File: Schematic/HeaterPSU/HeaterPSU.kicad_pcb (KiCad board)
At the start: 2 copper layers, 100 x 35 mm, 59 parts, among them J201 SMPS2_SEC, J202 Heater Output, J203 Heater Control, J204 MCU_Interface, J205 High voltage warning, K201 Relay_TE_OJT_SH_124DM, Q201 IRF4905, Q202 BSS138, SW201 SW_Rotary_1P5T_ALPSALPINE_SRBV, U201 TPS54302, U202 TLP185, U203 TLP185

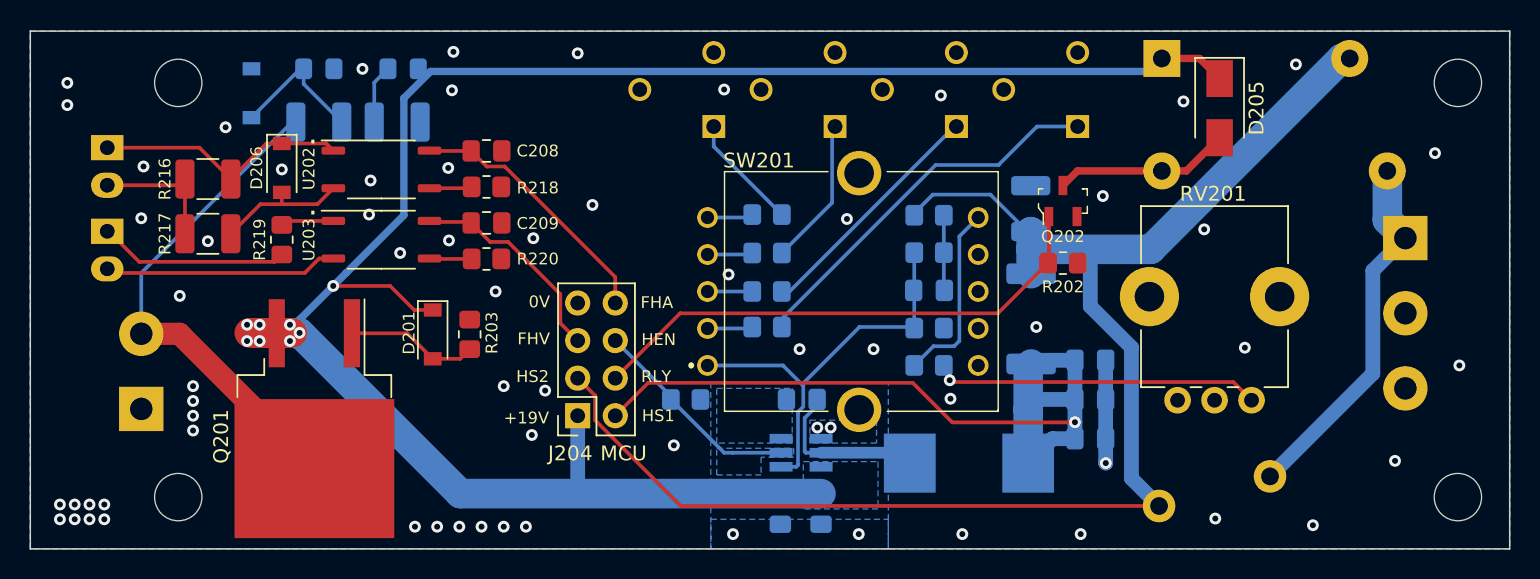
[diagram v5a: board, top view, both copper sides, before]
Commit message: Optocouplers moved to from PSU to MCU board
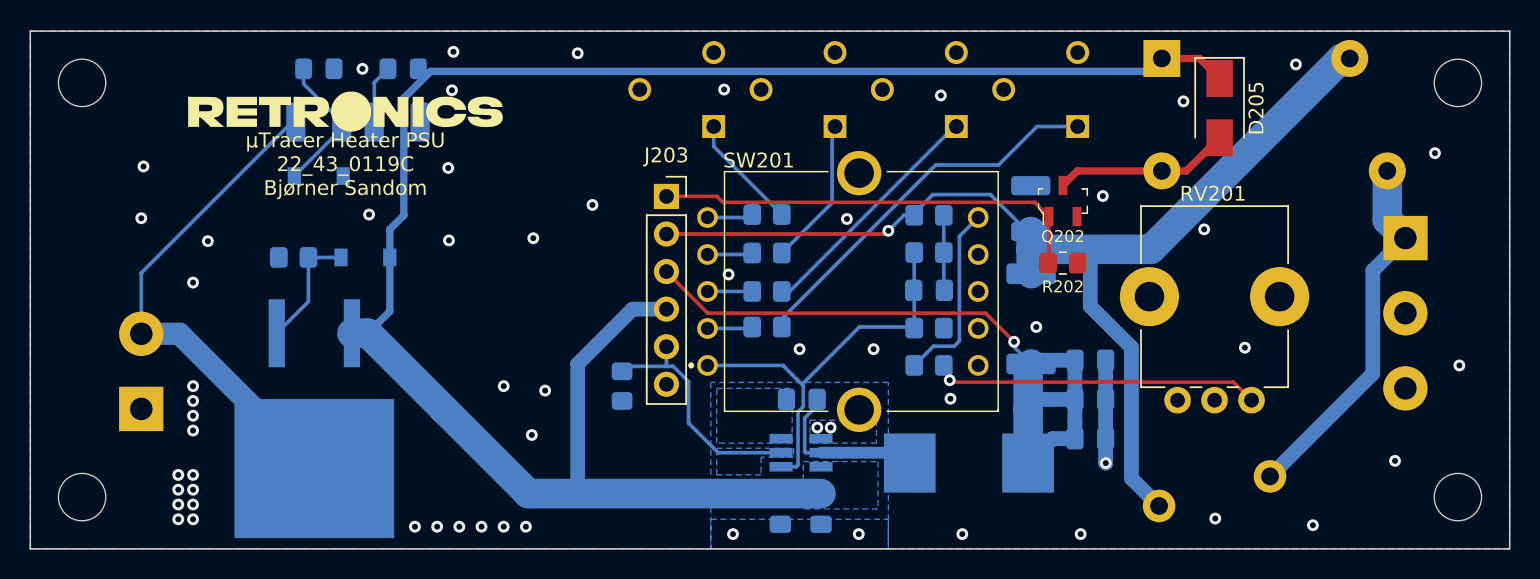
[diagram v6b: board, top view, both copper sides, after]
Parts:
- removed C208, C209: 220nF, Capacitor_SMD:C_0805_2012Metric_Pad1.18x1.45mm_HandSolder
- removed D206: 1N4148W, Diode_SMD:D_SOD-123
- removed J204: MCU_Interface, Connector_PinSocket_2.54mm:PinSocket_2x04_P2.54mm_Vertical
- removed J205: High voltage warning, myDevices:KF2510-2P
- removed R216, R217: 3.9kΩ 1/2W, Resistor_SMD:R_1210_3225Metric_Pad1.30x2.65mm_HandSolder
- removed R218, R219, R220: 220Ω, Resistor_SMD:R_0805_2012Metric_Pad1.20x1.40mm_HandSolder
- removed U202, U203: TLP185, Package_SO:SOIC-4_4.55x3.7mm_P2.54mm
- D201, Q201, R203: moved to B.Cu
- G***: moved to F.Cu
- J203: value Heater Control -> Conn_01x06; footprint myDevices:KF2510-2P -> Connector_PinSocket_2.54mm:PinSocket_1x06_P2.54mm_Vertical; moved to F.Cu
- moved J203 37.9 mm to (98.0, 56.2), turned to 0 degrees
- moved G*** 13.7 mm to (76.3, 50.4), turned to 0 degrees
- moved R203 13.0 mm to (72.8, 60.3), turned to 0 degrees
- moved D204 7.22 mm to (74.5, 54.8), turned to 180 degrees
- moved D201 6.91 mm to (77.7, 60.3), turned to 180 degrees
- moved H201 6.50 mm to (58.5, 48.5)
- moved H202 6.50 mm to (58.5, 76.5)
- moved R209 4.39 mm to (95.0, 69.0), turned to 90 degrees
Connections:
- J203 pad 1: Net-(D206-Pad1) -> RLY_CTRL
- J203 pad 2: Net-(J203-Pad2) -> HeaterSense2
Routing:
- net HeaterSense2: track 102.6 -> 76.0 mm, vias 0 -> 1
- net FlagMBHeaterActive: track 17.8 -> 0.00 mm
- net Net-(D206-Pad1): track 17.4 -> 0.00 mm
- net Net-(J205-Pad2): track 15.8 -> 0.00 mm
- net FlagHighVoltage: track 14.3 -> 0.00 mm
- net Net-(J205-Pad1): track 12.9 -> 0.00 mm
- net Net-(J203-Pad2): track 9.12 -> 0.00 mm
- net Net-(D206-Pad2): track 9.03 -> 0.00 mm
- net VDC: track 134.3 -> 126.3 mm, vias 8 -> 0
- net RLY_CTRL: track 35.7 -> 29.6 mm
- net HeaterSense1: track 55.6 -> 49.9 mm
- net Net-(R219-Pad1): track 3.60 -> 0.00 mm
- net Net-(R220-Pad2): track 2.82 -> 0.00 mm
- net Net-(R218-Pad2): track 2.76 -> 0.00 mm
- net Heater_EN: track 14.5 -> 16.3 mm
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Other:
- board text removed: "+ -"
- board text removed: "+19V"
- board text removed: "0V"
- board text removed: "FHA"
- board text removed: "FHV"
- board text removed: "HEN"
- board text removed: "HS1"
- board text removed: "HS2"
- board text removed: "HV LED"
- board text removed: "MB Heater"
- board text removed: "MCU"
- board text removed: "RLY"

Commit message: Added PWM controlled MOSFET output for soft start
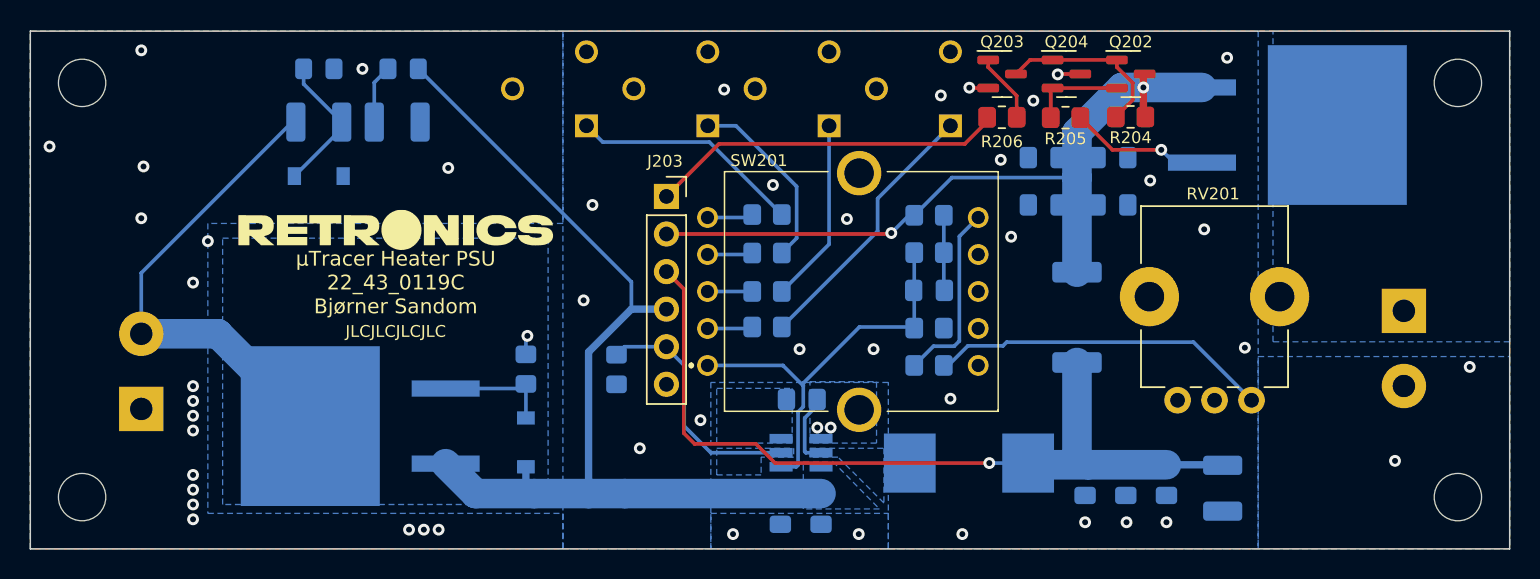
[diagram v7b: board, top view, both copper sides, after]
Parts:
- removed D205: MRA4005T3G, Diode_SMD:D_SMA
- removed K201: Relay_TE_OJT_SH_124DM, myDevices:Relay_TE_OJT_SH_124
- removed the R202 at (124.8, 60.7)
- removed the R209 at (95.0, 69.0)
- removed TH201: 25Ω 3.4A, myDevices:RV_Disc_D15.5mm_W4.5mm_P7.5mm
- added C201: 22µF 25V, Capacitor_SMD:C_0805_2012Metric_Pad1.18x1.45mm_HandSolder, B.Cu at (128.2, 53.5)
- added C203: 22µF 25V, Capacitor_SMD:C_0805_2012Metric_Pad1.18x1.45mm_HandSolder, B.Cu at (123.5, 56.8)
- added C204: 22µF 25V, Capacitor_SMD:C_0805_2012Metric_Pad1.18x1.45mm_HandSolder, B.Cu at (123.5, 53.5)
- added C206: 22µF 25V, Capacitor_SMD:C_0805_2012Metric_Pad1.18x1.45mm_HandSolder, B.Cu at (131.8, 75.3)
- added Q203: BC847, Package_TO_SOT_SMD:SOT-23, F.Cu at (120.7, 47.9)
- added Q204: BC857, Package_TO_SOT_SMD:SOT-23, F.Cu at (125.0, 47.9)
- added Q205: IRF9540N, Package_TO_SOT_SMD:TO-263-2, B.Cu at (140.0, 51.4)
- added R204: 4.7kΩ, Resistor_SMD:R_0805_2012Metric_Pad1.20x1.40mm_HandSolder, F.Cu at (129.4, 50.8)
- added R205: 100Ω, Resistor_SMD:R_0805_2012Metric_Pad1.20x1.40mm_HandSolder, F.Cu at (125.0, 50.9)
- added R206: 1kΩ, Resistor_SMD:R_0805_2012Metric_Pad1.20x1.40mm_HandSolder, F.Cu at (120.7, 50.8)
- added R211: 100kΩ, Resistor_SMD:R_0805_2012Metric_Pad1.20x1.40mm_HandSolder, B.Cu at (94.6, 67.9)
- J202: footprint myDevices:TerminalBlock_LCSC_P5.08mm_3 -> myDevices:TerminalBlock_LCSC_P5.08mm
- J203: value Conn_01x06 -> To MCU Board
- Q202: value BSS138 -> BC847; footprint digikey-footprints:SOT-23-3 -> Package_TO_SOT_SMD:SOT-23
- moved R208 22.9 mm to (135.6, 75.9), turned to -90 degrees
- moved R202 17.4 mm to (88.5, 67.8), turned to -90 degrees
- moved D201 16.6 mm to (88.5, 72.8), turned to 90 degrees
- moved C202 13.2 mm to (128.2, 56.8)
- moved Q202 9.73 mm to (129.4, 47.9), turned to 0 degrees
- moved G*** 8.69 mm to (79.7, 58.4)
- moved RV204 8.60 mm to (109.0, 51.4)
- moved RV205 8.60 mm to (117.2, 51.4)
- moved RV202 8.60 mm to (92.6, 51.4)
- moved RV203 8.60 mm to (100.8, 51.4)
- moved C208 8.11 mm to (126.3, 75.3), turned to 90 degrees
- moved J202 4.92 mm to (147.8, 63.9)
- moved C207 3.69 mm to (129.1, 75.3), turned to 90 degrees
- moved Q201 3.14 mm to (77.3, 71.7), turned to 180 degrees
- moved R207 3.10 mm to (125.8, 64.3)
- renumbered C201 to C205, C203 to C207, C204 to C208, C205 to C209, C206 to C210, C207 to C211, R203 to R202, R204 to R203, R205 to R207, R207 to R208, R206 to R209, R208 to R210, R210 to R212, R211 to R213, R212 to R214, R213 to R215, R214 to R216, R215 to R217
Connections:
- C202 pad 2: HeaterSense1 -> HeaterSense2
- J203 pad 1: RLY_CTRL -> Heater_PWM
- Q202 pad 1: RLY_CTRL -> Net-(Q202-Pad1)
- Q202 pad 2: GNDPWR -> Net-(Q202-Pad2)
- Q202 pad 3: Net-(D205-Pad2) -> HeaterSense2
- R208 pad 1: HeaterSense2 -> HeaterSense1
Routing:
- net VDC: track 126.3 -> 66.5 mm
- net RLY_CTRL: track 29.6 -> 0.00 mm
- net /HeaterOutput: track 24.9 -> 0.00 mm
- net HeaterSense2: track 76.0 -> 51.1 mm, vias 1 -> 2
- net Heater_PWM: track 0.00 -> 24.1 mm
- net Net-(Q202-Pad1): track 0.00 -> 12.0 mm
- net Net-(D205-Pad2): track 11.9 -> 0.00 mm
- net Net-(Q205-Pad1): track 0.00 -> 9.48 mm, vias 0 -> 1
- net Net-(R214-Pad2): track 7.86 -> 15.7 mm
- net Net-(R217-Pad2): track 25.9 -> 18.3 mm
- net Net-(Q202-Pad2): track 0.00 -> 6.40 mm
- net Net-(C205-Pad1): track 11.3 -> 5.01 mm
- net HeaterSense1: track 49.9 -> 54.9 mm
- net Net-(Q203-Pad1): track 0.00 -> 4.67 mm
- net Net-(R216-Pad2): track 16.4 -> 12.5 mm
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- added copper zone on B.Cu, net /HeaterOutput
- added copper zone on B.Cu, net Net-(C205-Pad1)
- added copper zone on B.Cu, net Net-(J201-Pad2)
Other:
- board text removed: "C F2 F1"

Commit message: Added 12V regulator for PWM output driver
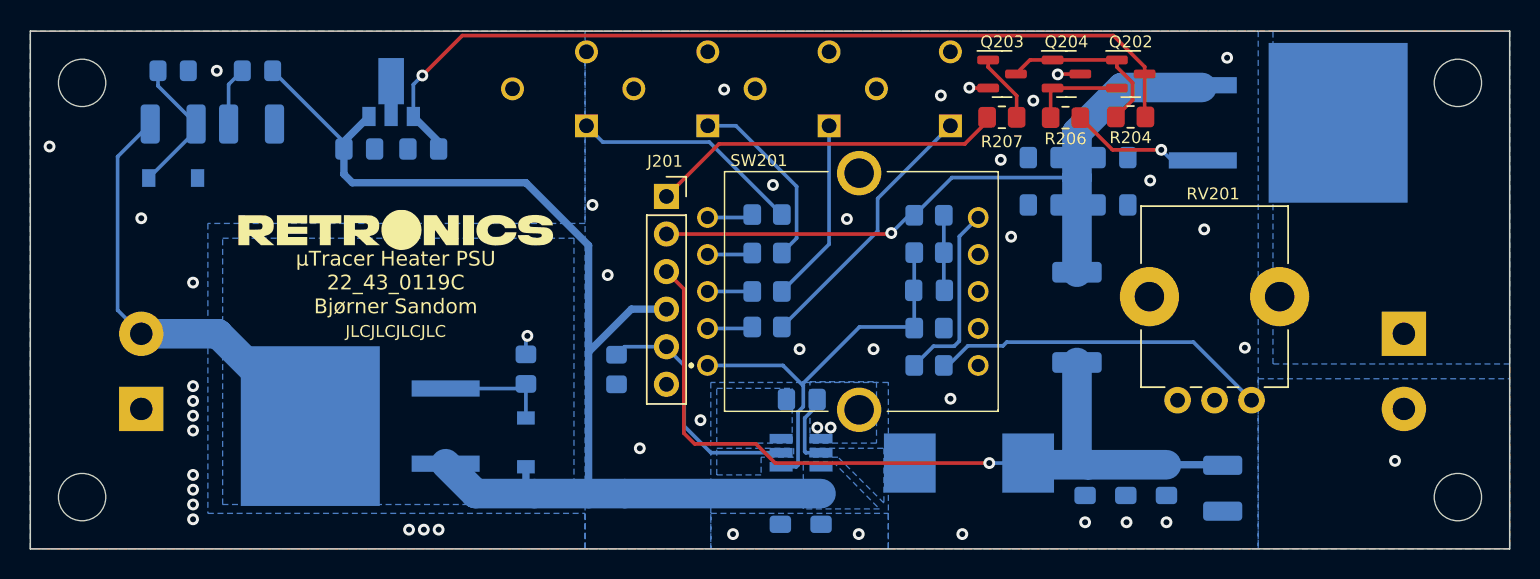
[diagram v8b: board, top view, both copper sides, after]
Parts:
- added C201: 10µF 50V, Capacitor_SMD:C_0805_2012Metric_Pad1.18x1.45mm_HandSolder, B.Cu at (77.2, 53.0)
- added C202: 100nF, Capacitor_SMD:C_0805_2012Metric_Pad1.18x1.45mm_HandSolder, B.Cu at (81.6, 53.0)
- added U201: L78L12_SOT89, Package_TO_SOT_SMD:SOT-89-3, B.Cu at (79.4, 49.1)
- Q205: value IRF9540N -> IRF4905
- R206: renamed from R205; value 100Ω -> 47Ω
- moved D202 9.85 mm to (70.4, 47.7)
- moved D203 9.85 mm to (64.7, 47.7)
- moved D204 9.85 mm to (64.7, 54.9)
- moved R201 9.85 mm to (64.7, 51.3)
- moved R203 9.85 mm to (70.0, 51.3)
- moved J203 1.55 mm to (147.8, 65.5)
- moved Q205 0.16 mm to (140.0, 51.2)
- renumbered C205 to C203, C206 to C204, C207 to C205, C208 to C206, C201 to C207, C202 to C208, C203 to C209, C204 to C210, C209 to C211, C210 to C212, C211 to C213, J203 to J201, J201 to J202, J202 to J203, R206 to R207, R207 to R208, R208 to R209, R209 to R210, R210 to R211, R211 to R212, R212 to R213, R213 to R214, R214 to R215, R215 to R216, R216 to R217, R217 to R218, U201 to U202
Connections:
- Q202 pad 3: HeaterSense2 -> Net-(Q202-Pad3)
- R204 pad 1: HeaterSense2 -> Net-(Q202-Pad3)
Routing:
- net Net-(Q202-Pad3): track 0.00 -> 60.2 mm, vias 0 -> 1
- net VDC: track 66.5 -> 81.9 mm
- net Net-(J202-Pad2): track 32.9 -> 29.8 mm
- net HeaterSense2: track 51.1 -> 48.5 mm, vias 2 -> 1
- net GNDPWR: vias 50 -> 45
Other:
- board text added: "+ 0"
- board text added: "DC Input"
- board text removed: "PSU2"
